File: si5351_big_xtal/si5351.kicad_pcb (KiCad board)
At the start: 2 copper layers, 15 parts, among them J1 PWR_IIC, J2 CLK0, J3 CLK1, J4 CLK2, U1 LD1117-3.3, U2 SI5351A, Y1 Crystal

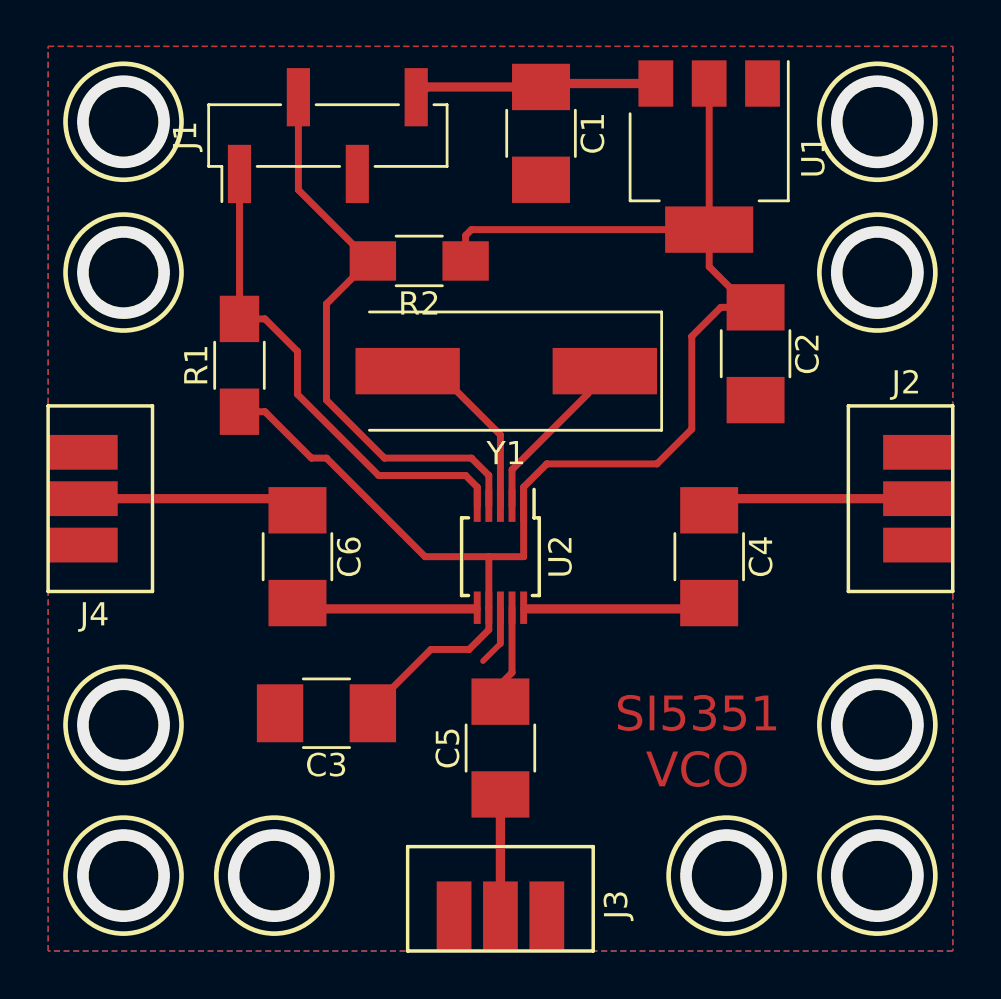
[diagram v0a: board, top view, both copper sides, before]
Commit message: Move CLK0 and CLK2 capacitors to reduce distortion
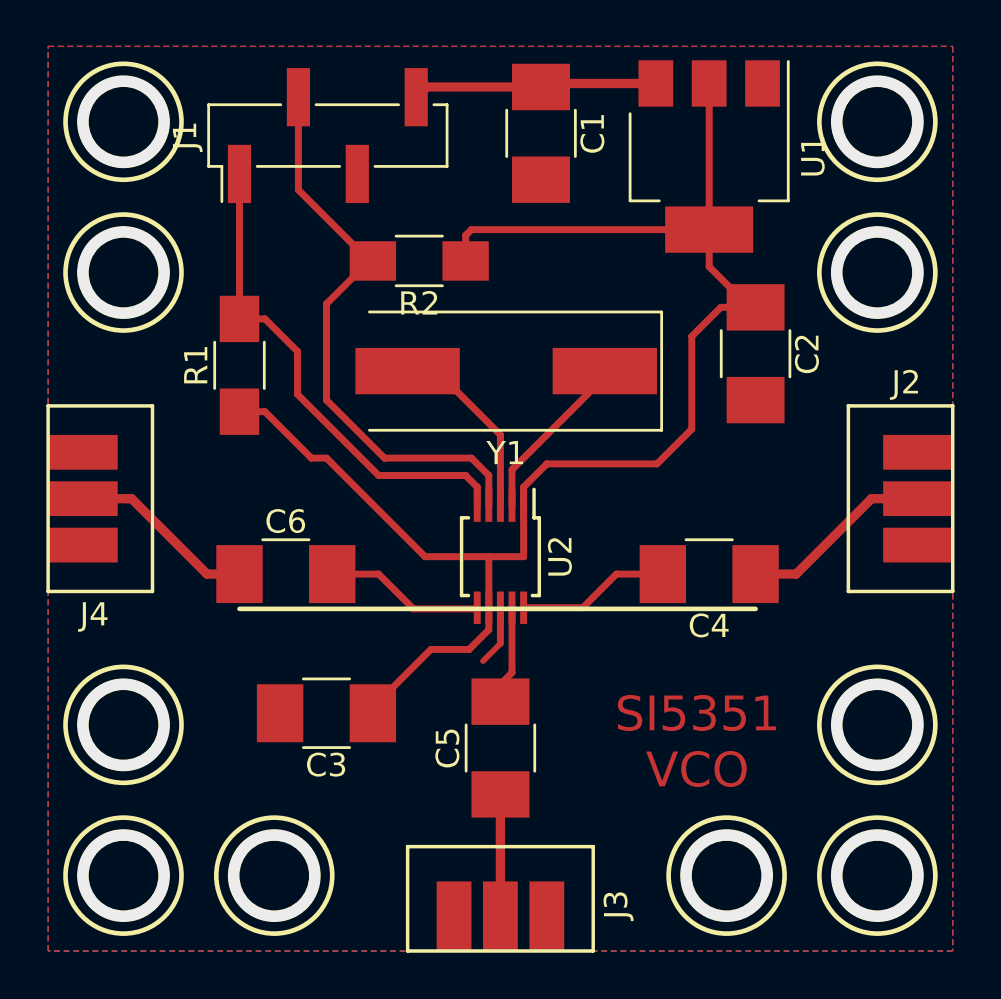
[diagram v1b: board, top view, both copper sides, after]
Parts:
- moved C6 0.90 mm to (27.0, 39.5), turned to 0 degrees
- moved C4 0.75 mm to (45.2, 39.5), turned to 180 degrees
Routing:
- net Net-(C6-Pad1): track 9.81 -> 8.10 mm
- net Net-(C4-Pad2): track 8.02 -> 6.60 mm
- net Net-(C4-Pad1): track 9.56 -> 8.35 mm
- net Net-(C6-Pad2): track 7.77 -> 6.89 mm
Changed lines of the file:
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@@
   (general
     (thickness 1.6)
-    (drawings 19)
-    (tracks 79)
+    (drawings 20)
+    (tracks 85)
     (zones 0)
     (modules 15)
@@
   )
   (module Capacitors_SMD:C_1210_HandSoldering (layer F.Cu)
-    (at 45.25 38.75 270)
+    (at 45.25 39.5 180)
     (descr "Capacitor SMD 1210, hand soldering")
     (tags "capacitor 1210")
     (attr smd)
-    (fp_text reference C4 (at 0 -2.25 270) (layer F.SilkS)
-      (effects (font (size 1 1) (thickness 0.15)))
-    )
-    (fp_text value 100n (at 0 2.5 270) (layer F.Fab)
+    (fp_text reference C4 (at 0 -2.25 180) (layer F.SilkS)
+      (effects (font (size 1 1) (thickness 0.15)))
+    )
+    (fp_text value 100n (at 0 2.5 180) (layer F.Fab)
       (effects (font (size 1 1) (thickness 0.15)))
     )
@@
     (fp_line (start 1.6 1.25) (end -1.6 1.25) (layer F.Fab) (width 0.1))
     (fp_line (start -1.6 1.25) (end -1.6 -1.25) (layer F.Fab) (width 0.1))
-    (fp_text user %R (at 0 -2.25 270) (layer F.Fab)
-      (effects (font (size 1 1) (thickness 0.15)))
-    )
-    (pad 2 smd rect (at 2 0 270) (size 2 2.5) (layers F.Cu F.Paste F.Mask)
+    (fp_text user %R (at 0 -2.25 180) (layer F.Fab)
+      (effects (font (size 1 1) (thickness 0.15)))
+    )
+    (pad 2 smd rect (at 2 0 180) (size 2 2.5) (layers F.Cu F.Paste F.Mask)
       (net 4 "Net-(C4-Pad2)"))
-    (pad 1 smd rect (at -2 0 270) (size 2 2.5) (layers F.Cu F.Paste F.Mask)
+    (pad 1 smd rect (at -2 0 180) (size 2 2.5) (layers F.Cu F.Paste F.Mask)
       (net 5 "Net-(C4-Pad1)"))
     (model Capacitors_SMD.3dshapes/C_1210.wrl
@@
   )
   (module Capacitors_SMD:C_1210_HandSoldering (layer F.Cu)
-    (at 27.5 38.75 270)
+    (at 27 39.5)
     (descr "Capacitor SMD 1210, hand soldering")
     (tags "capacitor 1210")
     (attr smd)
-    (fp_text reference C6 (at 0 -2.25 270) (layer F.SilkS)
-      (effects (font (size 1 1) (thickness 0.15)))
-    )
-    (fp_text value 100n (at 0 2.5 270) (layer F.Fab)
+    (fp_text reference C6 (at 0 -2.25) (layer F.SilkS)
+      (effects (font (size 1 1) (thickness 0.15)))
+    )
+    (fp_text value 100n (at 0 2.5) (layer F.Fab)
       (effects (font (size 1 1) (thickness 0.15)))
     )
@@
     (fp_line (start 1.6 1.25) (end -1.6 1.25) (layer F.Fab) (width 0.1))
     (fp_line (start -1.6 1.25) (end -1.6 -1.25) (layer F.Fab) (width 0.1))
-    (fp_text user %R (at 0 -2.25 270) (layer F.Fab)
-      (effects (font (size 1 1) (thickness 0.15)))
-    )
-    (pad 2 smd rect (at 2 0 270) (size 2 2.5) (layers F.Cu F.Paste F.Mask)
+    (fp_text user %R (at 0 -2.25) (layer F.Fab)
+      (effects (font (size 1 1) (thickness 0.15)))
+    )
+    (pad 2 smd rect (at 2 0) (size 2 2.5) (layers F.Cu F.Paste F.Mask)
       (net 8 "Net-(C6-Pad2)"))
-    (pad 1 smd rect (at -2 0 270) (size 2 2.5) (layers F.Cu F.Paste F.Mask)
+    (pad 1 smd rect (at -2 0) (size 2 2.5) (layers F.Cu F.Paste F.Mask)
       (net 9 "Net-(C6-Pad1)"))
     (model Capacitors_SMD.3dshapes/C_1210.wrl
@@
     )
   )
+  (gr_line (start 25 41) (end 47.25 41) (layer F.SilkS) (width 0.2))
   (gr_arc (start 52.5 20) (end 55.75 20) (angle -90) (layer Margin) (width 0.2))
   (gr_arc (start 52.5 52.5) (end 52.5 55.75) (angle -90) (layer Margin) (width 0.2))
@@
   (segment (start 44.5 33.25) (end 44.5 29.25) (width 0.3) (layer F.Cu) (net 3))
   (segment (start 44.5 29.25) (end 45.75 28) (width 0.3) (layer F.Cu) (net 3))
-  (segment (start 37.3 41) (end 37.25 40.95) (width 0.25) (layer F.Cu) (net 4))
-  (segment (start 45.25 41) (end 37.3 41) (width 0.4) (layer F.Cu) (net 4))
-  (segment (start 46 36.25) (end 45.25 37) (width 0.2) (layer F.Cu) (net 5))
-  (segment (start 54.5 36.25) (end 46 36.25) (width 0.4) (layer F.Cu) (net 5))
+  (segment (start 43.25 39.5) (end 41.25 39.5) (width 0.3) (layer F.Cu) (net 4))
+  (segment (start 39.8 40.95) (end 37.25 40.95) (width 0.3) (layer F.Cu) (net 4))
+  (segment (start 41.25 39.5) (end 39.8 40.95) (width 0.3) (layer F.Cu) (net 4))
+  (segment (start 49 39.5) (end 47.25 39.5) (width 0.4) (layer F.Cu) (net 5))
+  (segment (start 54.25 36.25) (end 52.25 36.25) (width 0.4) (layer F.Cu) (net 5))
+  (segment (start 52.25 36.25) (end 49 39.5) (width 0.4) (layer F.Cu) (net 5))
   (segment (start 36.25 50.7) (end 36.25 54.5) (width 0.4) (layer F.Cu) (net 6))
   (segment (start 36.25 49.5) (end 36.25 50.7) (width 0.4) (layer F.Cu) (net 6))
@@
   (segment (start 36.75 43.75) (end 36.75 40.95) (width 0.3) (layer F.Cu) (net 7))
   (segment (start 36.25 44.25) (end 36.75 43.75) (width 0.3) (layer F.Cu) (net 7))
-  (segment (start 35.2 41) (end 35.25 40.95) (width 0.25) (layer F.Cu) (net 8))
-  (segment (start 27.5 41) (end 35.2 41) (width 0.4) (layer F.Cu) (net 8))
-  (segment (start 26.75 36.25) (end 27.5 37) (width 0.2) (layer F.Cu) (net 9))
-  (segment (start 18 36.25) (end 26.75 36.25) (width 0.4) (layer F.Cu) (net 9))
+  (segment (start 35.2 41) (end 35.25 40.95) (width 0.3) (layer F.Cu) (net 8))
+  (segment (start 32.5 41) (end 35.2 41) (width 0.3) (layer F.Cu) (net 8))
+  (segment (start 31 39.5) (end 29 39.5) (width 0.3) (layer F.Cu) (net 8))
+  (segment (start 32.5 41) (end 31 39.5) (width 0.3) (layer F.Cu) (net 8))
+  (segment (start 20.15 36.25) (end 18.25 36.25) (width 0.4) (layer F.Cu) (net 9))
+  (segment (start 20.35 36.25) (end 20.15 36.25) (width 0.4) (layer F.Cu) (net 9))
+  (segment (start 23.6 39.5) (end 20.35 36.25) (width 0.4) (layer F.Cu) (net 9))
+  (segment (start 25 39.5) (end 23.6 39.5) (width 0.4) (layer F.Cu) (net 9))
   (segment (start 30.6 26) (end 30.75 26) (width 0.3) (layer F.Cu) (net 10))
   (segment (start 27.54 22.94) (end 30.6 26) (width 0.3) (layer F.Cu) (net 10))
